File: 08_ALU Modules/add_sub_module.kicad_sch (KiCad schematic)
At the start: 9 parts, among them U1 74LS00, U2 74LS32, U3 74LS32, U4 74LS86, U5 74LS283, U6 74LS245, U7 74LS86, U8 74LS86, U9 74LS283

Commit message: Alu control and modules completed, as well as Stack pointer module
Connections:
- net VCC: no longer U8.12, U8.13
- net ~{ADD}: now also U8.12; no longer U1.4
- net ~{SUB}: now also U8.13; no longer U1.5
- net at U8.11: now also U1.4, U1.5
- no-connect marks 3 -> 2
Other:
- moved on the sheet: U1B, U3D, U8C, U8D
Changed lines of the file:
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@@
 	(text "Add-Sub Module"
 		(exclude_from_sim no)
-		(at 123.444 21.844 0)
+		(at 149.86 137.668 0)
 		(effects
 			(font
@@
 	)
 	(junction
-		(at 208.28 153.67)
-		(diameter 0)
-		(color 0 0 0 0)
-	)
-	(junction
 		(at 40.64 106.68)
 		(diameter 0)
@@
 	)
 	(junction
-		(at 232.41 153.67)
+		(at 219.71 153.67)
 		(diameter 0)
 		(color 0 0 0 0)
@@
 	)
 	(junction
-		(at 256.54 153.67)
+		(at 243.84 153.67)
 		(diameter 0)
 		(color 0 0 0 0)
@@
 		(color 0 0 0 0)
 	)
-	(no_connect
-		(at 223.52 153.67)
+	(junction
+		(at 119.38 27.94)
+		(diameter 0)
+		(color 0 0 0 0)
 	)
 	(no_connect
-		(at 271.78 153.67)
+		(at 259.08 153.67)
 	)
 	(no_connect
-		(at 247.65 153.67)
+		(at 234.95 153.67)
 	)
 	(wire
@@
 	(wire
 		(pts
-			(xy 207.01 153.67) (xy 208.28 153.67)
+			(xy 203.2 62.23) (xy 209.55 62.23)
 		)
 		(stroke
@@
 	(wire
 		(pts
-			(xy 203.2 62.23) (xy 209.55 62.23)
+			(xy 180.34 71.12) (xy 181.61 71.12)
 		)
 		(stroke
@@
 	(wire
 		(pts
-			(xy 180.34 71.12) (xy 181.61 71.12)
+			(xy 40.64 137.16) (xy 43.18 137.16)
 		)
 		(stroke
@@
 	(wire
 		(pts
-			(xy 40.64 137.16) (xy 43.18 137.16)
+			(xy 102.87 25.4) (xy 104.14 25.4)
 		)
 		(stroke
@@
 	(wire
 		(pts
-			(xy 231.14 153.67) (xy 232.41 153.67)
+			(xy 218.44 153.67) (xy 219.71 153.67)
 		)
 		(stroke
@@
 	(wire
 		(pts
-			(xy 256.54 153.67) (xy 256.54 156.21)
+			(xy 243.84 153.67) (xy 243.84 156.21)
 		)
 		(stroke
@@
 	(wire
 		(pts
-			(xy 255.27 153.67) (xy 256.54 153.67)
+			(xy 242.57 153.67) (xy 243.84 153.67)
 		)
 		(stroke
@@
 	(wire
 		(pts
-			(xy 224.79 106.68) (xy 228.6 106.68)
+			(xy 119.38 27.94) (xy 119.38 30.48)
 		)
 		(stroke
@@
 	(wire
 		(pts
-			(xy 81.28 116.84) (xy 78.74 116.84)
+			(xy 224.79 106.68) (xy 228.6 106.68)
 		)
 		(stroke
@@
 	(wire
 		(pts
-			(xy 67.31 104.14) (xy 67.31 129.54)
+			(xy 81.28 116.84) (xy 78.74 116.84)
 		)
 		(stroke
@@
 	(wire
 		(pts
-			(xy 40.64 121.92) (xy 43.18 121.92)
+			(xy 67.31 104.14) (xy 67.31 129.54)
 		)
 		(stroke
@@
 	(wire
 		(pts
-			(xy 36.83 132.08) (xy 43.18 132.08)
+			(xy 40.64 121.92) (xy 43.18 121.92)
 		)
 		(stroke
@@
 	(wire
 		(pts
-			(xy 232.41 39.37) (xy 228.6 39.37)
+			(xy 36.83 132.08) (xy 43.18 132.08)
 		)
 		(stroke
@@
 	(wire
 		(pts
-			(xy 114.3 40.64) (xy 118.11 40.64)
+			(xy 232.41 39.37) (xy 228.6 39.37)
 		)
 		(stroke
@@
 	(wire
 		(pts
-			(xy 208.28 151.13) (xy 208.28 153.67)
+			(xy 43.18 40.64) (xy 40.64 40.64)
 		)
 		(stroke
@@
 	(wire
 		(pts
-			(xy 43.18 40.64) (xy 40.64 40.64)
+			(xy 119.38 30.48) (xy 120.65 30.48)
+		)
+		(stroke
+			(width 0)
+			(type default)
+		)
+	)
+	(wire
+		(pts
+			(xy 120.65 25.4) (xy 119.38 25.4)
 		)
 		(stroke
@@
 	(wire
 		(pts
-			(xy 232.41 153.67) (xy 232.41 156.21)
+			(xy 219.71 153.67) (xy 219.71 156.21)
 		)
 		(stroke
@@
 	(wire
 		(pts
-			(xy 232.41 151.13) (xy 232.41 153.67)
+			(xy 219.71 151.13) (xy 219.71 153.67)
 		)
 		(stroke
@@
 	(wire
 		(pts
+			(xy 119.38 25.4) (xy 119.38 27.94)
+		)
+		(stroke
+			(width 0)
+			(type default)
+		)
+	)
+	(wire
+		(pts
 			(xy 130.81 119.38) (xy 130.81 101.6)
 		)
@@
 	(wire
 		(pts
-			(xy 256.54 151.13) (xy 256.54 153.67)
+			(xy 243.84 151.13) (xy 243.84 153.67)
 		)
 		(stroke
@@
 	(wire
 		(pts
-			(xy 133.35 38.1) (xy 135.89 38.1)
-		)
-		(stroke
-			(width 0)
-			(type default)
-		)
-	)
-	(wire
-		(pts
 			(xy 224.79 119.38) (xy 228.6 119.38)
 		)
@@
 	(wire
 		(pts
-			(xy 114.3 35.56) (xy 118.11 35.56)
+			(xy 102.87 30.48) (xy 104.14 30.48)
 		)
 		(stroke
@@
 	(wire
 		(pts
-			(xy 135.89 38.1) (xy 135.89 50.8)
+			(xy 135.89 27.94) (xy 135.89 50.8)
 		)
 		(stroke
@@
 	(wire
 		(pts
-			(xy 208.28 153.67) (xy 208.28 156.21)
-		)
-		(stroke
-			(width 0)
-			(type default)
-		)
-	)
-	(wire
-		(pts
 			(xy 43.18 106.68) (xy 40.64 106.68)
 		)
@@
 	(hierarchical_label "~{ADD}"
 		(shape input)
-		(at 114.3 35.56 180)
+		(at 102.87 25.4 180)
 		(effects
 			(font
@@
 	(hierarchical_label "~{SUB}"
 		(shape input)
-		(at 114.3 40.64 180)
+		(at 102.87 30.48 180)
 		(effects
 			(font
@@
 	(hierarchical_label "VCC"
 		(shape input)
-		(at 207.01 153.67 180)
-		(effects
-			(font
-				(size 1.27 1.27)
-			)
-			(justify right)
-		)
-	)
-	(hierarchical_label "VCC"
-		(shape input)
 		(at 54.61 163.83 90)
 		(effects
@@
 	(hierarchical_label "VCC"
 		(shape input)
-		(at 231.14 153.67 180)
+		(at 218.44 153.67 180)
 		(effects
 			(font
@@
 	(hierarchical_label "VCC"
 		(shape input)
-		(at 255.27 153.67 180)
+		(at 242.57 153.67 180)
 		(effects
 			(font
@@
 	(symbol
 		(lib_id "74xx:74LS86")
-		(at 240.03 153.67 0)
+		(at 227.33 153.67 0)
 		(unit 3)
 		(exclude_from_sim no)
@@
 		(fields_autoplaced yes)
 		(property "Reference" "U8"
-			(at 239.7252 144.78 0)
+			(at 227.0252 144.78 0)
 			(effects
 				(font
@@
 		)
 		(property "Value" "74LS86"
-			(at 239.7252 147.32 0)
+			(at 227.0252 147.32 0)
 			(effects
 				(font
@@
 		)
 		(property "Footprint" "Package_DIP:DIP-14_W7.62mm"
-			(at 240.03 153.67 0)
+			(at 227.33 153.67 0)
 			(effects
 				(font
@@
 		)
 		(property "Datasheet" "74xx/74ls86.pdf"
-			(at 240.03 153.67 0)
+			(at 227.33 153.67 0)
 			(effects
 				(font
@@
 		)
 		(property "Description" "Quad 2-input XOR"
-			(at 240.03 153.67 0)
+			(at 227.33 153.67 0)
 			(effects
 				(font
@@
 	(symbol
 		(lib_id "74xx:74LS00")
-		(at 125.73 38.1 0)
+		(at 128.27 27.94 0)
 		(unit 2)
 		(exclude_from_sim no)
@@
 		(fields_autoplaced yes)
 		(property "Reference" "U1"
-			(at 125.7217 29.21 0)
+			(at 128.2617 19.05 0)
 			(effects
 				(font
@@
 		)
 		(property "Value" "74LS00"
-			(at 125.7217 31.75 0)
+			(at 128.2617 21.59 0)
 			(effects
 				(font
@@
 		)
 		(property "Footprint" "Package_DIP:DIP-14_W7.62mm"
-			(at 125.73 38.1 0)
+			(at 128.27 27.94 0)
 			(effects
 				(font
@@
 		)
 		(property "Datasheet" "http://www.ti.com/lit/gpn/sn74ls00"
-			(at 125.73 38.1 0)
+			(at 128.27 27.94 0)
 			(effects
 				(font
@@
 		)
 		(property "Description" "quad 2-input NAND gate"
-			(at 125.73 38.1 0)
+			(at 128.27 27.94 0)
 			(effects
 				(font
@@
 	(symbol
 		(lib_id "74xx:74LS86")
-		(at 215.9 153.67 0)
+		(at 111.76 27.94 0)
 		(unit 4)
 		(exclude_from_sim no)
@@
 		(fields_autoplaced yes)
 		(property "Reference" "U8"
-			(at 215.5952 144.78 0)
+			(at 111.4552 19.05 0)
 			(effects
 				(font
@@
 		)
 		(property "Value" "74LS86"
-			(at 215.5952 147.32 0)
+			(at 111.4552 21.59 0)
 			(effects
 				(font
@@
 		)
 		(property "Footprint" "Package_DIP:DIP-14_W7.62mm"
-			(at 215.9 153.67 0)
+			(at 111.76 27.94 0)
 			(effects
 				(font
@@
 		)
 		(property "Datasheet" "74xx/74ls86.pdf"
-			(at 215.9 153.67 0)
+			(at 111.76 27.94 0)
 			(effects
 				(font
@@
 		)
 		(property "Description" "Quad 2-input XOR"
-			(at 215.9 153.67 0)
+			(at 111.76 27.94 0)
 			(effects
 				(font
@@
 	(symbol
 		(lib_id "74xx:74LS32")
-		(at 264.16 153.67 0)
+		(at 251.46 153.67 0)
 		(unit 4)
 		(exclude_from_sim no)
@@
 		(fields_autoplaced yes)
 		(property "Reference" "U3"
-			(at 264.16 144.78 0)
+			(at 251.46 144.78 0)
 			(effects
 				(font
@@
 		)
 		(property "Value" "74LS32"
-			(at 264.16 147.32 0)
+			(at 251.46 147.32 0)
 			(effects
 				(font
@@
 		)
 		(property "Footprint" "Package_DIP:DIP-14_W7.62mm"
-			(at 264.16 153.67 0)
+			(at 251.46 153.67 0)
 			(effects
 				(font
@@
 		)
 		(property "Datasheet" "http://www.ti.com/lit/gpn/sn74LS32"
-			(at 264.16 153.67 0)
+			(at 251.46 153.67 0)
 			(effects
 				(font
@@
 		)
 		(property "Description" "Quad 2-input OR"
-			(at 264.16 153.67 0)
+			(at 251.46 153.67 0)
 			(effects
 				(font

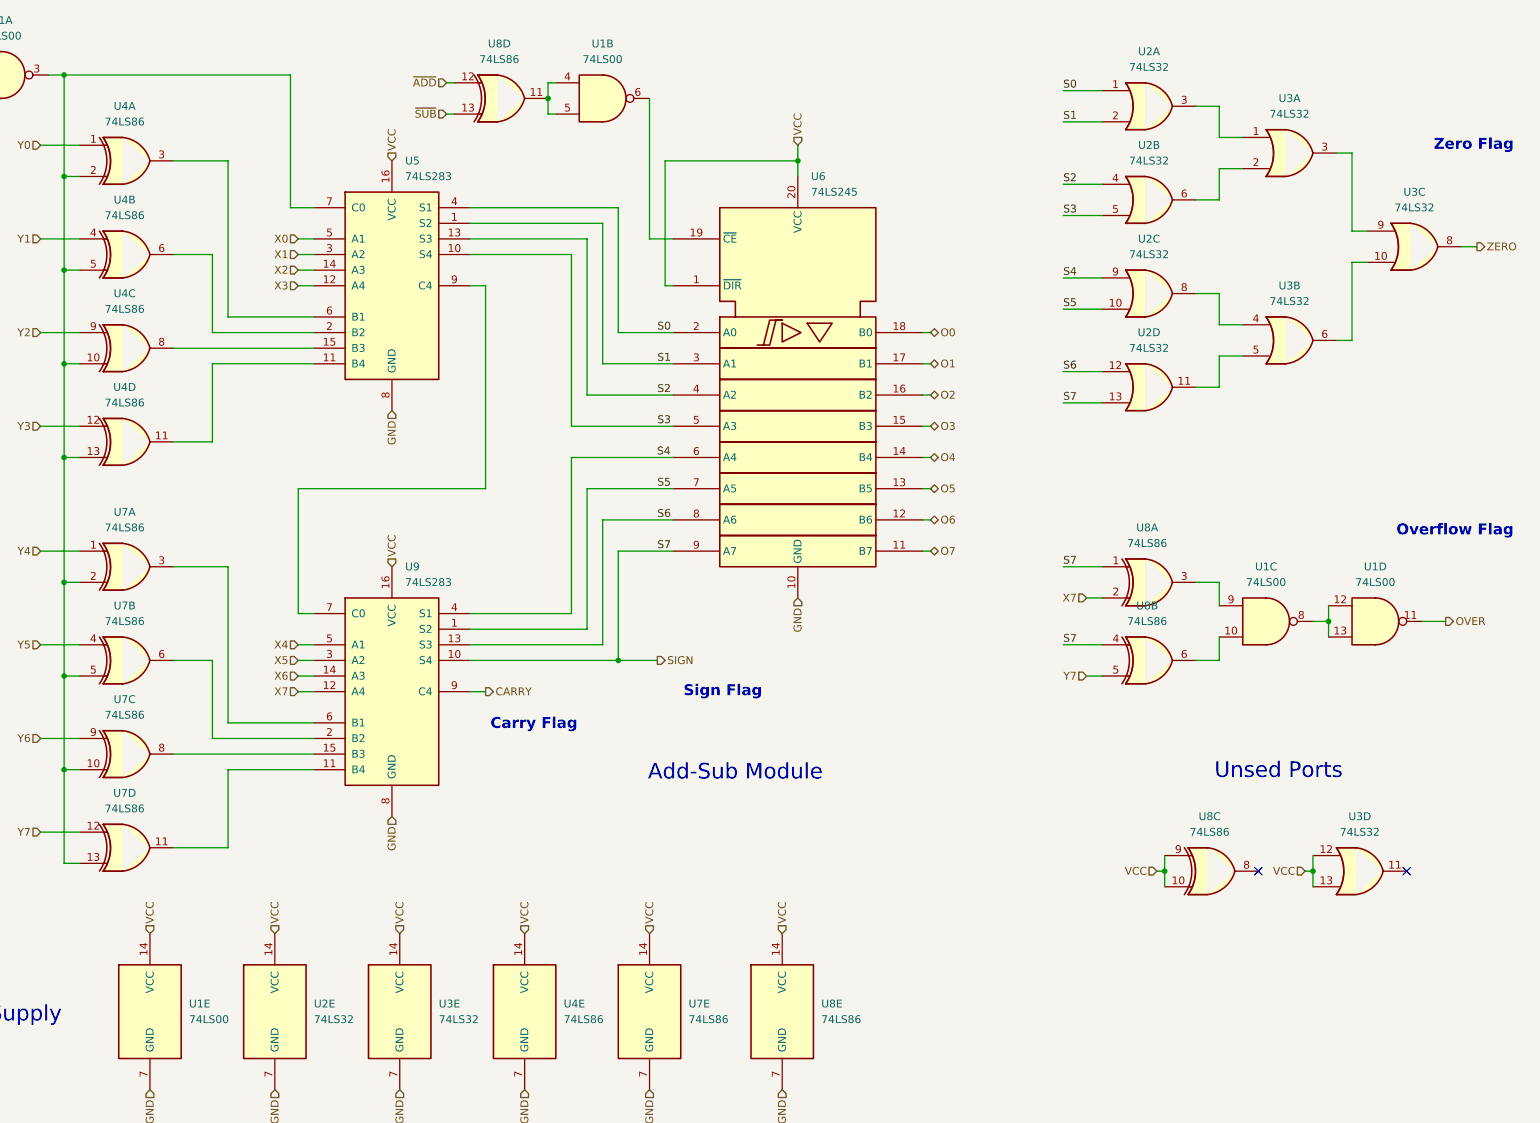
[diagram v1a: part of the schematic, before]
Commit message: Last revision of the cpu, all boards have been ordered. Implementation to be tested and documented in following commits.
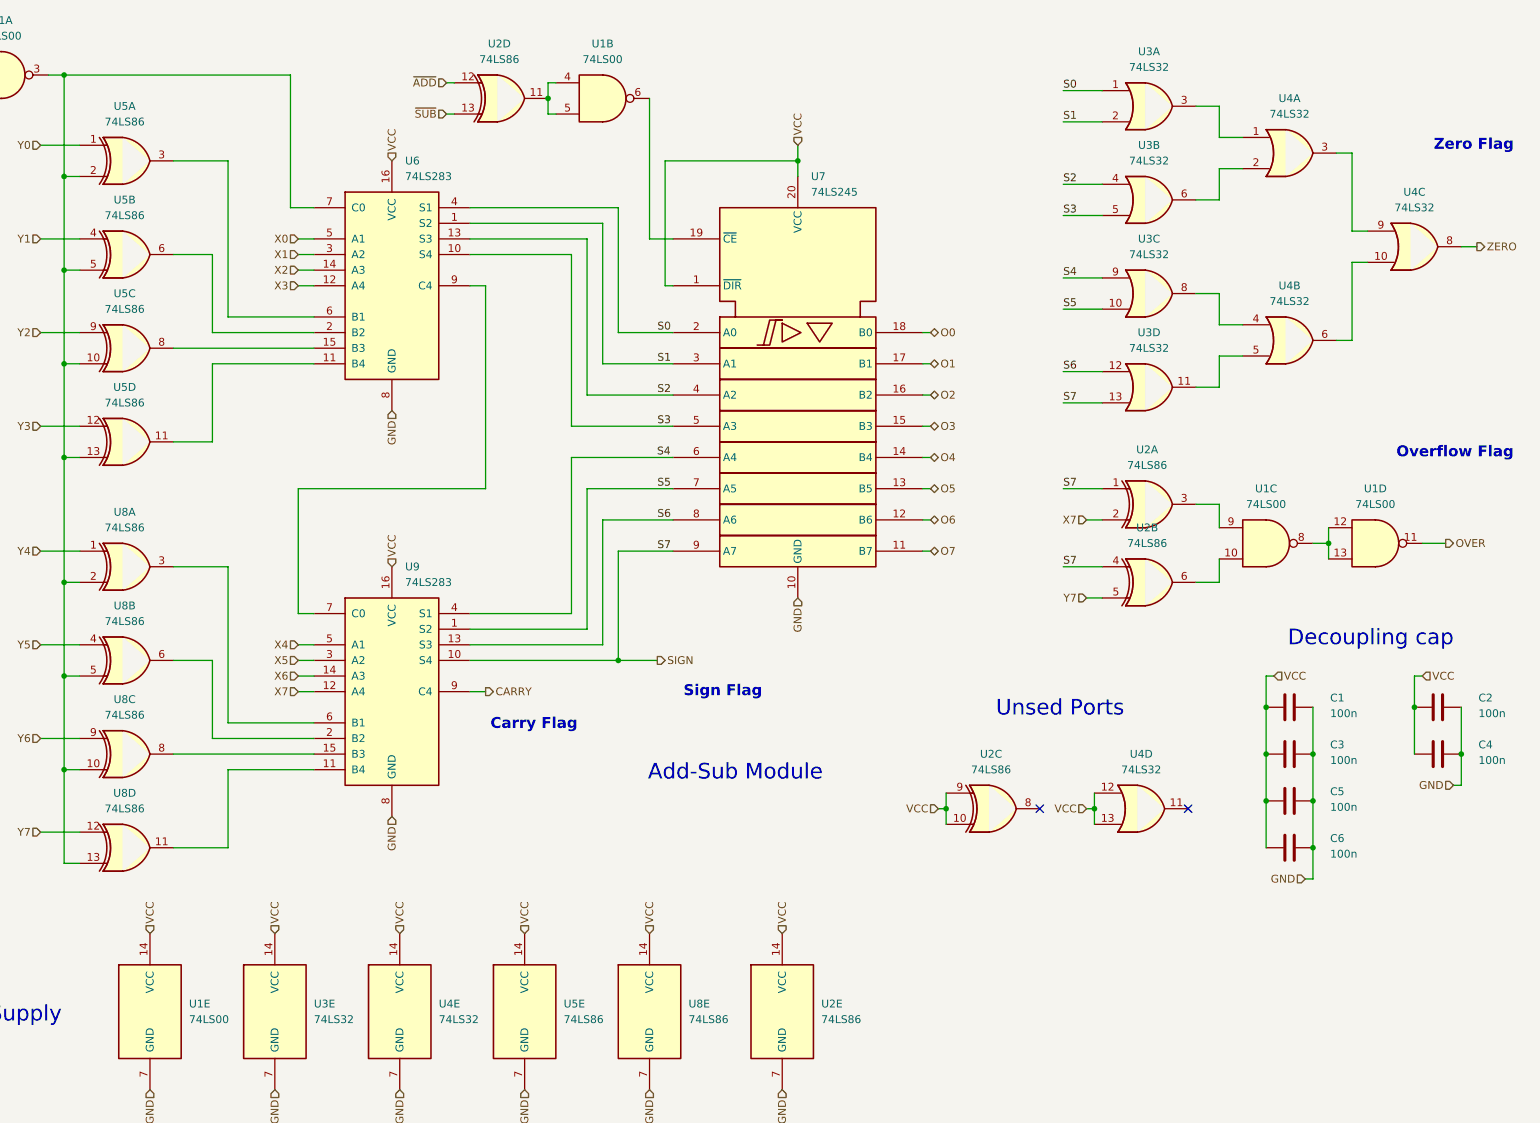
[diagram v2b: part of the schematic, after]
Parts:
- added C1, C2, C3, C4, C5, C6: 100n, Capacitor_THT:C_Disc_D3.0mm_W1.6mm_P2.50mm, symbol Device:C
- renumbered U8 to U2, U2 to U3, U3 to U4, U4 to U5, U5 to U6, U6 to U7, U7 to U8
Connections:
- net GND: now also C1.2, C2.2, C3.2, C4.2, C5.2, C6.2
- net VCC: now also C1.1, C2.1, C3.1, C4.1, C5.1, C6.1
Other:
- note added: "Decoupling cap"
- moved on the sheet: U1C, U1D, U2A, U2B, U2C, U4D
